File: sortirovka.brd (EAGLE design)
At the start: 160 x 100 mm, 19 parts, among them U1 MAX3485CSA, X1 PI3-CON, X2 MKDSN1,5/2-5,08, X3 MKDSN1,5/4-5,08, X4 MKDSN1,5/2-5,08

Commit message: rev1
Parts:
- added D5, D6: BAV199, diode:SOT23
- added G1: CR2032H, MyLib:CR2032H
- added IC1: DS1307Z, MyLib:SOIC8
- added OC1, OC2: (no value), MyLib:SMD4
- added Q5: (no value), MyLib:MA306
- added R10, R11: 3k3, rcl:R0805
- added R5, R6: 10k, rcl:R0805
- added R7: 0, rcl:R0805
- added R8, R9: 100, rcl:R0805
- added U$1, U$2: NSI45020AT1GSOD-123, MyLib:SOD123
- added U$3: NUP2105LSOT23-R, MyLib:SOT23-R
- added X5: MKDSN1,5/3-5,08, con-phoenix-508:MKDSN1,5/3-5,08
- added X6, X8: 22-23-2051, con-molex:22-23-2051
- added X7: 22-23-2041, con-molex:22-23-2041
- R1, R2, R3, R4: value (none) -> 10k
- moved X4 31.6 mm to (91.2, 24.1), turned to 180 degrees
- moved X2 27.4 mm to (93.8, 93.6), turned to 0 degrees
- moved D1 21.5 mm to (109.5, 36.2)
- moved D2 21.5 mm to (109.5, 41.3)
- moved D3 21.5 mm to (109.5, 46.4)
- moved D4 21.5 mm to (109.5, 51.4)
- moved X3 20.2 mm to (102.4, 43.8)
- moved C2 18.1 mm to (91.1, 54.3), turned to 0 degrees
- moved Q1 14.8 mm to (93.5, 35.2)
- moved Q2 14.8 mm to (93.5, 40.2)
- moved Q3 14.8 mm to (93.5, 45.3)
- moved R1 14.8 mm to (88.5, 35.2)
- moved R2 14.8 mm to (88.6, 40.3)
- moved R4 14.8 mm to (88.8, 50.4)
- moved Q4 14.8 mm to (93.4, 50.3)
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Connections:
- new net +5V: IC1.8
- new net MISO: X1.P$21, X6.4, X8.4
- new net MOSI: X1.P$19, X6.5, X8.5
- new net N$14: R7.1, X1.P$1, X1.P$17
- new net N$15: OC2.4, R6.2, X1.P$31
- new net N$16: OC1.1, U$1.C
- new net N$17: OC2.1, U$2.C
- new net N$18: OC1.4, R5.2, X1.P$29
- new net N$19: D5.3, R8.1, U$1.A
- new net N$20: G1.+, IC1.3
- new net N$21: R8.2, X5.3
- new net N$22: R9.2, X5.1
- new net N$23: IC1.1, Q5.1
- new net N$24: D6.3, R9.1, U$2.A
- new net N$25: IC1.2, Q5.4
- new net N$26: IC1.6, R10.1, X1.P$5, X7.2
- new net N$27: IC1.5, R11.1, X1.P$3, X7.1
- new net SPI0: X1.P$24, X6.2
- new net SPI1: X1.P$26, X8.2
- new net SPI_CLK: X1.P$23, X6.3, X8.3
- net +24V: now also D5.2, D6.2
- net +3V3: now also OC1.3, OC2.3, R10.2, R11.2, R7.2, X7.3; no longer X1.P$1, X1.P$17
- net GND: now also D5.1, D6.1, G1.-, IC1.4, OC1.2, OC2.2, R5.1, R6.1, U$3.3, X1.P$14, X1.P$25, X5.2, X6.1, X7.4, X8.1
- net N$4: now also U$3.2, U1.6; no longer U1.7
- net N$5: now also U$3.1, U1.7; no longer U1.6
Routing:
- net GND: track 0.00 -> 367.8 mm
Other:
- board size 160 x 100 mm -> 79.4 x 80.9 mm

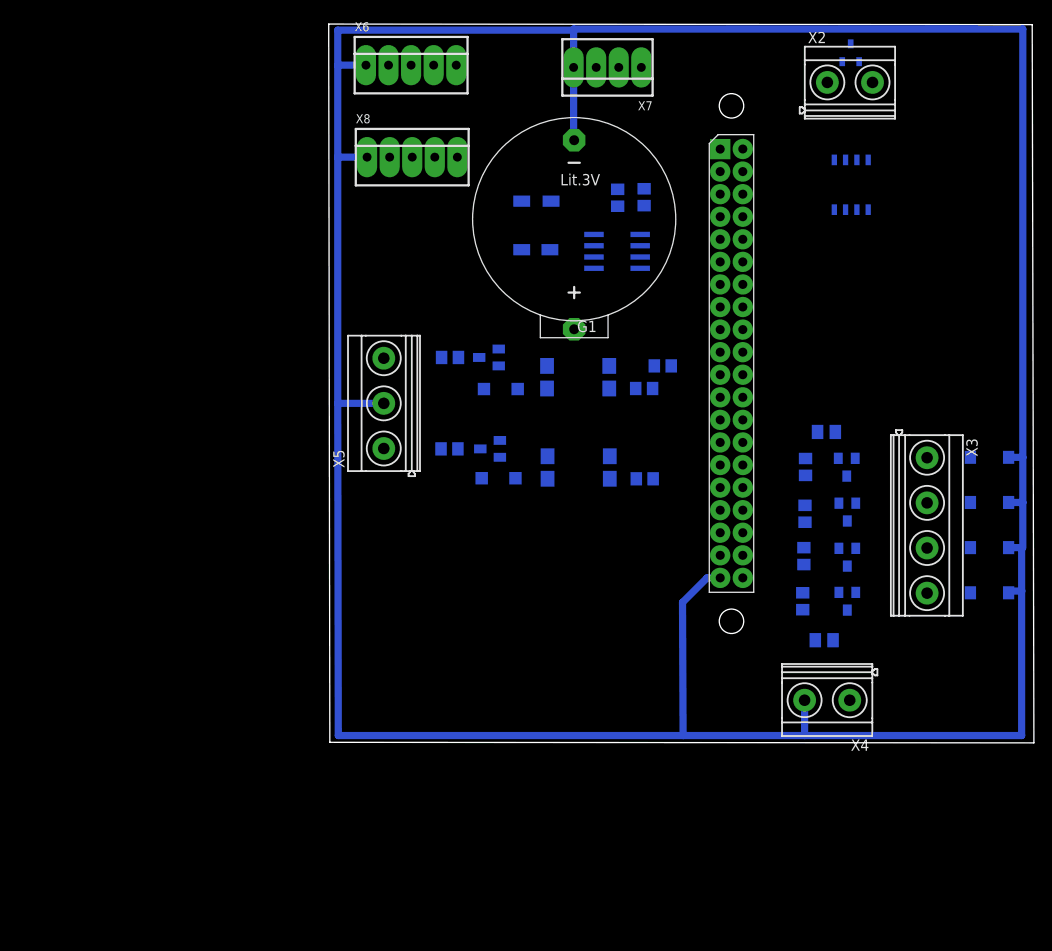
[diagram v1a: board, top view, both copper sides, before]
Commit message: rev2 5-input 4-output
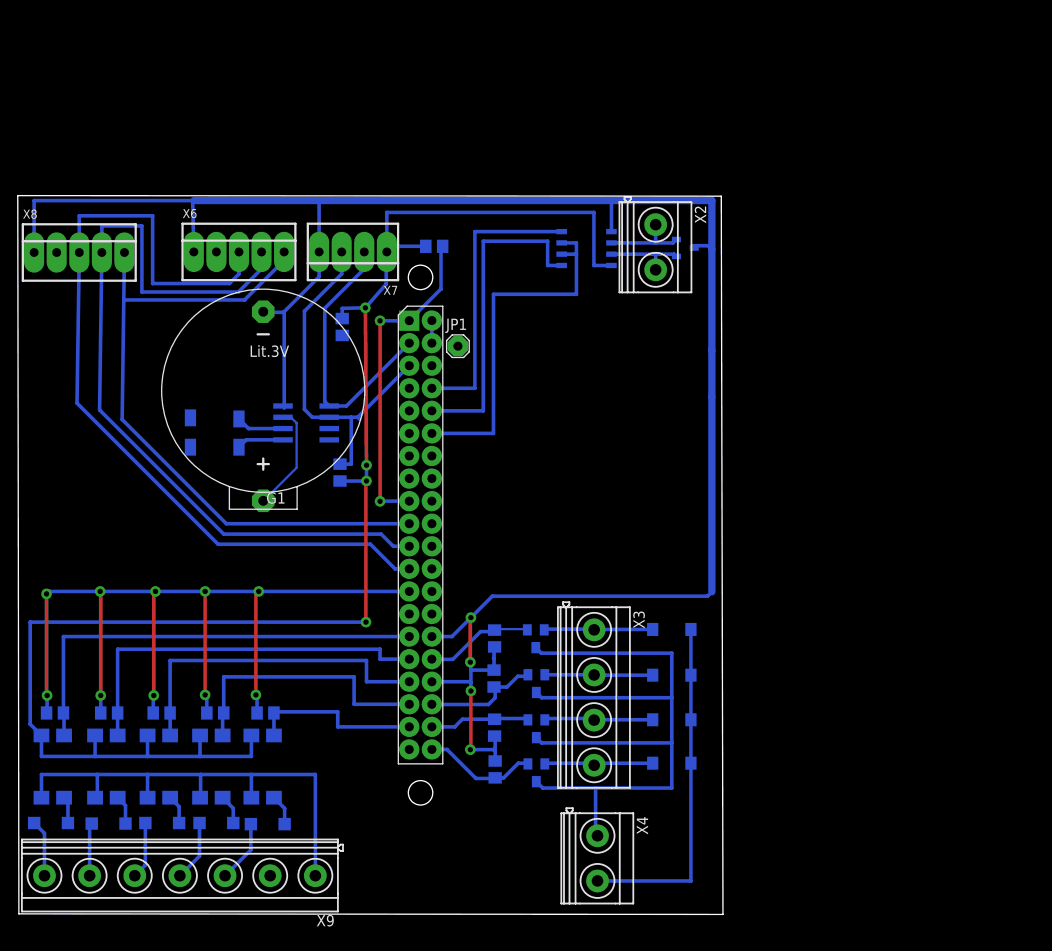
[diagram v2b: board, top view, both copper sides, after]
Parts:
- removed C1, C2: (no value), rcl:C0805K
- removed D5, D6: BAV199, diode:SOT23
- removed X5: MKDSN1,5/3-5,08, con-phoenix-508:MKDSN1,5/3-5,08
- added JP1: (no value), pinhead:1X01
- added OC3, OC4, OC5: (no value), MyLib:SMD4
- added R12: 10k, rcl:R0805
- added U$4, U$5, U$6: NSI45020AT1GSOD-123, MyLib:SOD123
- added X9: MKDSN1,5/7-5,08, con-phoenix-508:MKDSN1,5/7-5,08
- R8, R9: value 100 -> 10k
- moved R5 75.7 mm to (4.32, 22.7), turned to 180 degrees
- moved OC1 73.6 mm to (4.06, 16.6), turned to 0 degrees
- moved U$1 70.3 mm to (3.87, 10.3)
- moved R6 65.8 mm to (10.4, 22.7), turned to 180 degrees
- moved OC2 62.9 mm to (10.1, 16.6), turned to 0 degrees
- moved U$2 58.6 mm to (10.4, 10.2)
- moved R8 51.5 mm to (16.3, 22.7), turned to 180 degrees
- moved D3 46.2 mm to (73.7, 17.0)
- moved R10 44.0 mm to (36.4, 49.7), turned to 270 degrees
- moved Q5 42.7 mm to (22.5, 53.8), turned to 0 degrees
- moved X3 42.2 mm to (65.0, 24.4)
- moved D2 40.7 mm to (73.7, 21.9)
- moved D4 40.7 mm to (73.7, 32.1)
- moved G1 40.0 mm to (27.7, 58.9)
- moved X1 40.0 mm to (45.0, 76.5)
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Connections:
- new net GND1: D1.A, D2.A, D3.A, D4.A, OC1.2, OC2.2, OC3.2, OC4.2, OC5.2, X4.2, X9.1
- new net N$28: JP1.1, X1.P$2, X1.P$4
- new net N$29: OC4.4, R9.2, X1.P$35
- new net N$30: OC4.1, U$5.C
- new net N$31: OC5.4, R12.2, X1.P$37
- new net N$32: OC5.1, U$6.C
- new net N$33: U$5.A, X9.4
- new net N$35: U$4.A, X9.5
- new net N$37: U$6.A, X9.3
- net +24V: no longer C1.1, C2.1, D5.2, D6.2
- net +3V3: now also OC3.3, OC4.3, OC5.3, X7.1; no longer X7.3
- net GND: now also R12.1, R8.1, R9.1; no longer C1.2, C2.2, D1.A, D2.A, D3.A, D4.A, D5.1, D6.1, OC1.2, OC2.2, X4.2, X5.2
- net N$11: now also D1.C; no longer D3.C
- net N$13: now also D3.C; no longer D1.C
- net N$19: now also OC3.4, R8.2, X1.P$33; no longer D5.3, R8.1, U$1.A
- net N$21: now also U$1.A, X9.7; no longer R8.2, X5.3
- net N$22: now also U$2.A, X9.6; no longer R9.2, X5.1
- net N$24: now also OC3.1, U$4.C; no longer D6.3, R9.1, U$2.A
- net N$26: now also X7.3; no longer X7.2
- net N$27: now also X7.2; no longer X7.1
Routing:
- net +3V3: track 0.00 -> 176.2 mm, vias 0 -> 4
- net SPI_CLK: track 0.00 -> 94.7 mm
- net GND1: track 0.00 -> 94.4 mm
- net MISO: track 0.00 -> 90.3 mm
- net +24V: track 0.00 -> 82.8 mm
- net MOSI: track 0.00 -> 76.9 mm
- net N$18: track 0.00 -> 50.1 mm
- net N$15: track 0.00 -> 43.6 mm
- net N$3: track 0.00 -> 41.0 mm
- net N$26: track 0.00 -> 40.9 mm
- net N$19: track 0.00 -> 37.7 mm
- net N$14: track 0.00 -> 37.1 mm, vias 0 -> 2
- net N$2: track 0.00 -> 36.4 mm
- net N$1: track 0.00 -> 32.2 mm
- net N$27: track 0.00 -> 31.6 mm
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
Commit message: rev1.0 to produce
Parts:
- removed JP1: (no value), pinhead:1X01
- removed Q1, Q2, Q3, Q4: (no value), MyLib:SOT23-WIDE
- removed X2: MKDSN1,5/2-5,08, con-phoenix-508:MKDSN1,5/2-5,08
- added C1, C2, C4: (no value), rcl:SANYO-OSCON_C
- added C10, C3, C5, C6, C7, C8, C9: 0.1, rcl:C0805
- added D10, D5, D6, D7, D8, D9: DIODE1N4007, MyLib:SMA-DIODE
- added IC3: LM1117IMPX-3.3, lm1117:SOT223
- added JP2: (no value), pinhead:1X01
- added OC10, OC6, OC7, OC8, OC9: (no value), MyLib:SMD4
- added R13: 10k, rcl:R0805
- added R14: 0, rcl:R0805
- added R15: 120, rcl:0204/7
- added R16, R17: 47, rcl:0204/7
- added R18, R19, R20: 560, rcl:0204/7
- added U$7: NSI45020AT1GSOD-123, MyLib:SOD123
- added X10: MKDSN1,5/3-5,08, con-phoenix-508:MKDSN1,5/3-5,08
- added X5: 22-23-2021, con-molex:22-23-2021
- R1, R2, R3, R4: value 10k -> 200
- moved R11 25.0 mm to (18.3, 49.1), turned to 180 degrees
- moved D4 24.9 mm to (71.1, 7.30), turned to 90 degrees
- moved X3 23.9 mm to (64.9, 0.51), turned to 180 degrees
- moved D3 22.0 mm to (54.0, 7.30), turned to 90 degrees
- moved D1 21.3 mm to (65.3, 7.30), turned to 90 degrees
- moved IC1 21.1 mm to (11.6, 53.0)
- moved R4 20.4 mm to (72.1, 22.1), turned to 180 degrees
- moved D2 20.3 mm to (59.6, 7.24), turned to 90 degrees
- moved G1 20.2 mm to (13.2, 44.9), turned to 0 degrees
- moved X4 20.1 mm to (46.1, 0.57), turned to 180 degrees
- moved R10 18.4 mm to (18.4, 53.6), turned to 180 degrees
- moved X6 16.1 mm to (9.27, 71.4)
- moved Q5 13.6 mm to (11.6, 45.7), turned to 180 degrees
- moved R3 13.4 mm to (66.3, 22.0), turned to 180 degrees
- moved X8 10.5 mm to (9.27, 64.3)
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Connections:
- removed net +5V: IC1.8
- removed net N$31: OC5.4, R12.2, X1.P$37
- new net N$34: OC6.4, R13.2, X1.P$37
- new net N$36: D10.C, OC6.1, U$7.C
- new net N$38: U$7.A, X9.2
- new net N$39: OC5.4, R12.2, X1.P$35
- new net N$40: OC4.4, R9.2, X1.P$33
- new net N$41: OC3.4, R8.2, X1.P$31
- new net N$42: OC2.4, R6.2, X1.P$29
- new net N$43: JP2.1, OC1.4, R5.2, X1.P$7
- new net N$45: R15.2, R16.1, X10.2
- new net N$46: R15.1, R17.1, X10.1
- new net N$47: R17.2, R19.1, U$3.2, U1.6
- new net PW: C2.+, C3.1, IC3.3, R14.2, X5.1
- net +24V: now also C4.+, C6.1, OC10.3, OC7.3, OC8.3, OC9.3; no longer Q1.3, Q2.3, Q3.3, Q4.3
- net +3V3: now also C1.+, C10.1, C5.1, C7.1, C8.1, C9.1, IC1.8, IC3.2, IC3.TAB, OC6.3, R19.2
- net GND: now also C1.-, C10.2, C2.-, C3.2, C5.2, C7.2, C8.2, C9.2, IC3.1, OC10.2, OC7.2, OC8.2, OC9.2, R13.1, R18.1, R20.2, X5.2, X6.5, X8.5; no longer R1.1, R2.1, R3.1, R4.1, X6.1, X8.1
- net GND1: now also C4.-, C6.2, D10.A, D5.A, D6.A, D7.A, D8.A, D9.A, OC6.2
- net MISO: now also X6.2, X8.2; no longer X6.4, X8.4
- net MOSI: now also X6.3, X8.3; no longer X6.5, X8.5
- net N$10: now also OC10.4; no longer Q4.2
- net N$11: now also OC9.4; no longer Q3.2
- net N$12: now also OC8.4; no longer Q2.2
- net N$13: now also OC7.4; no longer Q1.2
- net N$15: now also OC7.1, R1.1; no longer OC2.4, R6.2, X1.P$31
- net N$16: now also D5.C
- net N$17: now also D6.C
- net N$18: now also OC8.1, R2.1; no longer OC1.4, R5.2, X1.P$29
- net N$19: now also OC9.1, R3.1; no longer OC3.4, R8.2, X1.P$33
- net N$24: now also D7.C
- net N$28: now also R14.1; no longer JP1.1
- net N$29: now also OC10.1, R4.1; no longer OC4.4, R9.2, X1.P$35
- net N$30: now also D8.C
- net N$32: now also D9.C
- net N$4: now also R16.2, R18.2, U$3.1, U1.7; no longer U$3.2, U1.6, X2.1
- net N$5: now also R20.1, X10.3; no longer U$3.1, U1.7, X2.2
- net N$6: no longer Q1.1
- net N$7: no longer Q2.1
- net N$8: no longer Q3.1
- net N$9: no longer Q4.1
- net SPI0: now also X6.4; no longer X6.2
- net SPI1: now also X8.4; no longer X8.2
- net SPI_CLK: now also X6.1, X8.1; no longer X6.3, X8.3
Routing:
- net GND1: track 94.4 -> 227.5 mm
- net PW: track 0.00 -> 70.9 mm
- net +3V3: track 176.2 -> 239.9 mm
- net N$18: track 50.1 -> 2.41 mm
- net N$27: track 31.6 -> 76.3 mm
- net N$15: track 43.6 -> 2.47 mm
- net N$42: track 0.00 -> 40.0 mm
- net N$19: track 37.7 -> 2.41 mm
- net N$41: track 0.00 -> 34.7 mm
- net +24V: track 82.8 -> 50.8 mm
- net N$40: track 0.00 -> 29.2 mm
- net N$29: track 30.7 -> 2.47 mm
- net N$14: track 37.1 -> 11.7 mm, vias 2 -> 0
- net N$26: track 40.9 -> 65.2 mm
- net N$39: track 0.00 -> 23.0 mm
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- added copper zone on layer 16, net GND
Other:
- board size 79.4 x 80.9 mm -> 86.8 x 85.8 mm

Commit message: some changes in packages
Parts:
- C1, C2, C4: device rcl:SANYO-OSCON_C -> rcl:E3,5-8
- R15, R16, R17, R18, R19, R20: device rcl:0204/7 -> rcl:0207/10
- moved C6 9.06 mm to (47.1, 12.6)
- moved C7 6.41 mm to (60.5, 69.0)
- moved C2 6.11 mm to (57.4, 51.8), turned to 0 degrees
- moved IC3 4.50 mm to (56.7, 59.9)
- moved C1 4.27 mm to (57.5, 66.0), turned to 0 degrees
- moved R14 3.49 mm to (47.2, 73.2)
- moved R7 3.36 mm to (45.0, 73.2)
- moved R16 2.03 mm to (64.6, 63.2)
- moved R17 1.91 mm to (70.4, 72.3)
- moved U$3 1.72 mm to (70.4, 73.1)
- moved R20 1.68 mm to (67.4, 54.7)
- moved C4 1.68 mm to (46.8, 9.91), turned to 180 degrees
- moved C3 1.53 mm to (56.7, 54.3)
- moved R18 1.52 mm to (68.2, 63.2)
- moved R19 1.28 mm to (70.5, 75.8)
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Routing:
- net N$14: track 11.7 -> 5.80 mm
- net GND1: track 227.5 -> 232.6 mm
- net N$45: track 17.8 -> 22.4 mm
- net GND: track 362.0 -> 365.9 mm
- net N$28: track 12.0 -> 8.20 mm
- net +3V3: track 239.9 -> 243.3 mm
- net N$46: track 10.0 -> 7.25 mm
- net PW: track 70.9 -> 72.7 mm
- net +24V: track 50.8 -> 52.0 mm
- net N$5: track 6.64 -> 7.40 mm

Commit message: rev 1.1 to produce
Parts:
- removed JP2: (no value), pinhead:1X01
- OC1, OC10, OC2, OC3, OC4, OC5, OC6, OC7, OC8, OC9: device MyLib:SMD4 -> MyLib:SFH6106
- R16, R17: value 47 -> 15
- R18, R19: value 560 -> 1k5
- R20: value 560 -> 10
- moved C5 13.3 mm to (20.1, 47.2), turned to 270 degrees
- moved C6 12.3 mm to (52.2, 1.46), turned to 270 degrees
- moved C8 12.0 mm to (0.64, 66.6), turned to 270 degrees
- moved C9 11.4 mm to (6.10, 38.1), turned to 180 degrees
- moved IC1 6.77 mm to (17.5, 56.3)
- moved R4 4.91 mm to (75.8, 25.3), turned to 90 degrees
- moved R1 4.88 mm to (50.8, 19.5), turned to 270 degrees
- moved R10 4.80 mm to (22.7, 51.5), turned to 270 degrees
- moved OC10 4.76 mm to (77.1, 16.9)
- moved D4 4.71 mm to (75.8, 6.92)
- moved R5 4.54 mm to (3.87, 30.2)
- moved R6 4.45 mm to (10.4, 30.2)
- moved R3 4.33 mm to (68.8, 25.6), turned to 90 degrees
- moved R8 4.22 mm to (17.0, 30.2)
- moved R13 4.12 mm to (37.0, 30.2)
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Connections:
- net N$43: no longer JP2.1
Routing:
- net GND: track 365.9 -> 217.7 mm, vias 10 -> 12
- net N$43: track 7.73 -> 57.5 mm, vias 0 -> 2
- net +3V3: track 243.3 -> 262.8 mm, vias 4 -> 2
- net N$6: track 16.2 -> 4.10 mm
- net +24V: track 52.0 -> 64.0 mm
- net N$27: track 76.3 -> 65.8 mm
- net N$7: track 21.2 -> 14.1 mm
- net GND1: track 232.6 -> 225.8 mm
- net N$44: track 0.00 -> 5.08 mm
- net N$25: track 13.2 -> 8.14 mm
- net N$46: track 7.25 -> 12.2 mm
- net N$26: track 65.2 -> 69.0 mm
- net N$34: track 10.0 -> 12.9 mm
- net N$8: track 26.0 -> 23.3 mm
- net N$20: track 7.87 -> 5.21 mm
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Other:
- board size 86.8 x 85.8 mm -> 86.7 x 86.7 mm

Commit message: manufacture-1
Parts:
- R12, R13, R5, R6, R8, R9: value 10k -> 1k
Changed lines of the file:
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@@
 <element name="OC1" library="MyLib" package="SFH6106" value="" x="3.556" y="22.0345" rot="MR0"/>
 <element name="OC2" library="MyLib" package="SFH6106" value="" x="10.033" y="22.0345" rot="MR0"/>
-<element name="R5" library="rcl" package="R0805" value="10k" x="3.8735" y="30.1625" rot="MR180"/>
-<element name="R6" library="rcl" package="R0805" value="10k" x="10.3505" y="30.226" rot="MR180"/>
+<element name="R5" library="rcl" package="R0805" value="1k" x="3.8735" y="30.1625" rot="MR180"/>
+<element name="R6" library="rcl" package="R0805" value="1k" x="10.3505" y="30.226" rot="MR180"/>
 <element name="U$1" library="MyLib" package="SOD123" value="NSI45020AT1GSOD-123" x="2.921" y="13.9065" rot="MR0"/>
 <element name="U$2" library="MyLib" package="SOD123" value="NSI45020AT1GSOD-123" x="9.779" y="13.9065" rot="MR0"/>
@@
 <element name="D3" library="MyLib" package="SMA-DIODE" value="DIODE1N4007" x="53.975" y="7.239" rot="MR90"/>
 <element name="OC3" library="MyLib" package="SFH6106" value="" x="16.7005" y="22.2885" rot="MR0"/>
-<element name="R8" library="rcl" package="R0805" value="10k" x="17.018" y="30.1625" rot="MR180"/>
+<element name="R8" library="rcl" package="R0805" value="1k" x="17.018" y="30.1625" rot="MR180"/>
 <element name="U$4" library="MyLib" package="SOD123" value="NSI45020AT1GSOD-123" x="16.764" y="13.97" rot="MR0"/>
 <element name="OC4" library="MyLib" package="SFH6106" value="" x="23.368" y="22.098" rot="MR0"/>
-<element name="R9" library="rcl" package="R0805" value="10k" x="23.6855" y="30.1625" rot="MR180"/>
+<element name="R9" library="rcl" package="R0805" value="1k" x="23.6855" y="30.1625" rot="MR180"/>
 <element name="U$5" library="MyLib" package="SOD123" value="NSI45020AT1GSOD-123" x="23.749" y="13.9065" rot="MR0"/>
 <element name="OC5" library="MyLib" package="SFH6106" value="" x="30.0355" y="22.098" rot="MR0"/>
-<element name="R12" library="rcl" package="R0805" value="10k" x="30.353" y="30.1625" rot="MR180"/>
+<element name="R12" library="rcl" package="R0805" value="1k" x="30.353" y="30.1625" rot="MR180"/>
 <element name="U$6" library="MyLib" package="SOD123" value="NSI45020AT1GSOD-123" x="30.5435" y="13.9065" rot="MR0"/>
 <element name="D5" library="MyLib" package="SMA-DIODE" value="DIODE1N4007" x="7.0485" y="7.239" rot="MR90"/>
@@
 <element name="D9" library="MyLib" package="SMA-DIODE" value="DIODE1N4007" x="31.8135" y="7.239" rot="MR90"/>
 <element name="OC6" library="MyLib" package="SFH6106" value="" x="36.6395" y="22.1615" rot="MR0"/>
-<element name="R13" library="rcl" package="R0805" value="10k" x="36.957" y="30.1625" rot="MR180"/>
+<element name="R13" library="rcl" package="R0805" value="1k" x="36.957" y="30.1625" rot="MR180"/>
 <element name="U$7" library="MyLib" package="SOD123" value="NSI45020AT1GSOD-123" x="37.2745" y="13.9065" rot="MR0"/>
 <element name="D10" library="MyLib" package="SMA-DIODE" value="DIODE1N4007" x="37.973" y="7.239" rot="MR90"/>
